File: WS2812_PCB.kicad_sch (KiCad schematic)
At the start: 4 parts, among them J1 OUT, J2 IN

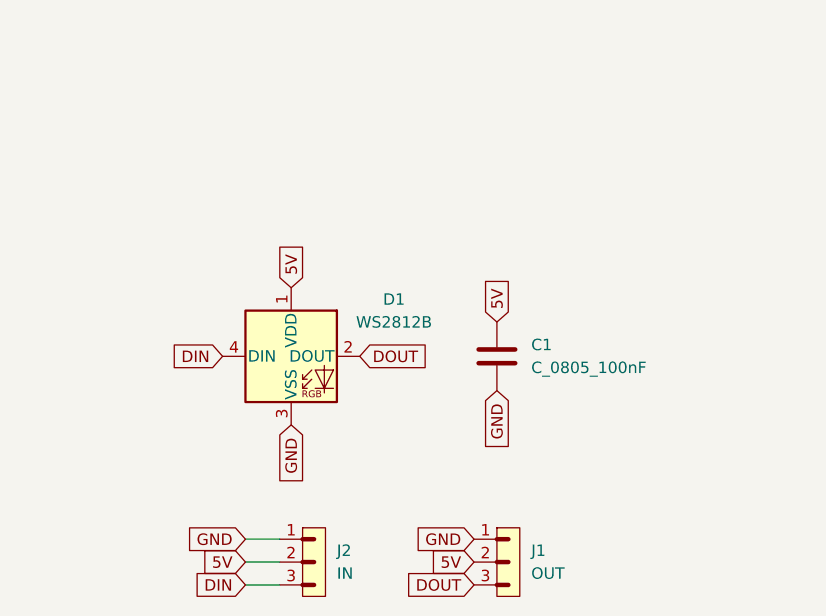
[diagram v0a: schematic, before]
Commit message: Se modifican los archivos de la pcb y esquematico para generar los archivos pdf
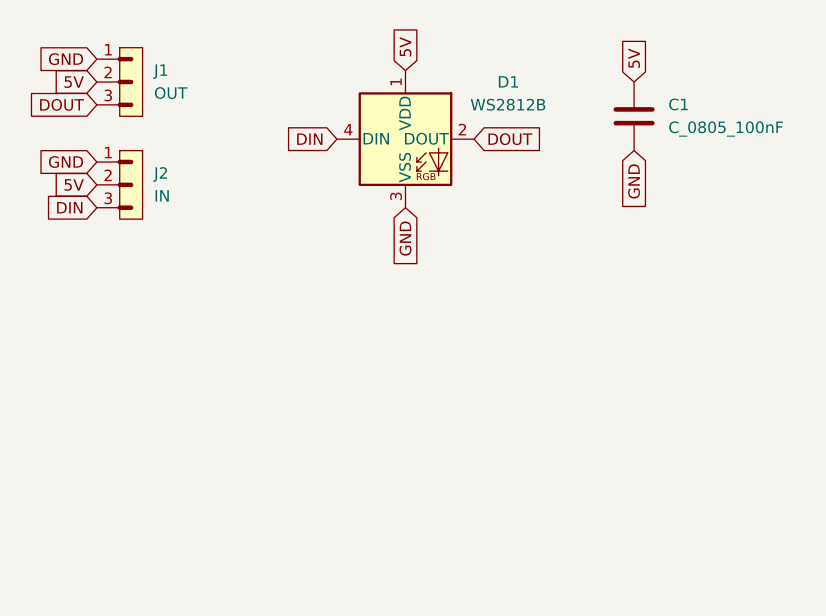
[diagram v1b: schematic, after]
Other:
- company: (none) -> Dan Angles
- title: (none) -> WS2812 PCB
- moved on the sheet: C1, D1, J1, J2
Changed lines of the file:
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@@
 	(generator "eeschema")
 	(generator_version "8.0")
-	(paper "A4")
-	(wire
-		(pts
-			(xy 58.42 80.01) (xy 62.23 80.01)
-		)
-		(stroke
-			(width 0)
-			(type default)
-		)
-	)
-	(wire
-		(pts
-			(xy 58.42 77.47) (xy 62.23 77.47)
-		)
-		(stroke
-			(width 0)
-			(type default)
-		)
-	)
-	(wire
-		(pts
-			(xy 58.42 82.55) (xy 62.23 82.55)
-		)
-		(stroke
-			(width 0)
-			(type default)
-		)
+	(paper "User" 150 100)
+	(title_block
+		(title "WS2812 PCB")
+		(date "2024-05-28")
+		(rev "1.0")
+		(company "Dan Angles")
 	)
 	(global_label "5V"
 		(shape input)
-		(at 63.5 49.53 90)
+		(at 76.2 25.4 90)
 		(fields_autoplaced yes)
 		(effects
@@
 		)
 		(property "Intersheetrefs" "${INTERSHEET_REFS}"
-			(at 63.5 44.2467 90)
+			(at 76.2 20.1167 90)
 			(effects
 				(font
@@
 	(global_label "5V"
 		(shape input)
-		(at 83.82 80.01 180)
-		(fields_autoplaced yes)
-		(effects
-			(font
-				(size 1.27 1.27)
-			)
-			(justify right)
-		)
-		(property "Intersheetrefs" "${INTERSHEET_REFS}"
-			(at 78.5367 80.01 0)
+		(at 41.91 26.67 180)
+		(fields_autoplaced yes)
+		(effects
+			(font
+				(size 1.27 1.27)
+			)
+			(justify right)
+		)
+		(property "Intersheetrefs" "${INTERSHEET_REFS}"
+			(at 36.6267 26.67 0)
 			(effects
 				(font
@@
 	(global_label "DOUT"
 		(shape input)
-		(at 71.12 57.15 0)
+		(at 83.82 33.02 0)
 		(fields_autoplaced yes)
 		(effects
@@
 		)
 		(property "Intersheetrefs" "${INTERSHEET_REFS}"
-			(at 79.0038 57.15 0)
+			(at 91.7038 33.02 0)
 			(effects
 				(font
@@
 	(global_label "5V"
 		(shape input)
-		(at 58.42 80.01 180)
-		(fields_autoplaced yes)
-		(effects
-			(font
-				(size 1.27 1.27)
-			)
-			(justify right)
-		)
-		(property "Intersheetrefs" "${INTERSHEET_REFS}"
-			(at 53.1367 80.01 0)
+		(at 41.91 38.1 180)
+		(fields_autoplaced yes)
+		(effects
+			(font
+				(size 1.27 1.27)
+			)
+			(justify right)
+		)
+		(property "Intersheetrefs" "${INTERSHEET_REFS}"
+			(at 36.6267 38.1 0)
 			(effects
 				(font
@@
 	(global_label "5V"
 		(shape input)
-		(at 86.36 53.34 90)
+		(at 101.6 26.67 90)
 		(fields_autoplaced yes)
 		(effects
@@
 		)
 		(property "Intersheetrefs" "${INTERSHEET_REFS}"
-			(at 86.36 48.0567 90)
+			(at 101.6 21.3867 90)
 			(effects
 				(font
@@
 	(global_label "DOUT"
 		(shape input)
-		(at 83.82 82.55 180)
-		(fields_autoplaced yes)
-		(effects
-			(font
-				(size 1.27 1.27)
-			)
-			(justify right)
-		)
-		(property "Intersheetrefs" "${INTERSHEET_REFS}"
-			(at 75.9362 82.55 0)
+		(at 41.91 29.21 180)
+		(fields_autoplaced yes)
+		(effects
+			(font
+				(size 1.27 1.27)
+			)
+			(justify right)
+		)
+		(property "Intersheetrefs" "${INTERSHEET_REFS}"
+			(at 34.0262 29.21 0)
 			(effects
 				(font
@@
 	(global_label "GND"
 		(shape input)
-		(at 83.82 77.47 180)
-		(fields_autoplaced yes)
-		(effects
-			(font
-				(size 1.27 1.27)
-			)
-			(justify right)
-		)
-		(property "Intersheetrefs" "${INTERSHEET_REFS}"
-			(at 76.9643 77.47 0)
+		(at 41.91 24.13 180)
+		(fields_autoplaced yes)
+		(effects
+			(font
+				(size 1.27 1.27)
+			)
+			(justify right)
+		)
+		(property "Intersheetrefs" "${INTERSHEET_REFS}"
+			(at 35.0543 24.13 0)
 			(effects
 				(font
@@
 	(global_label "GND"
 		(shape input)
-		(at 63.5 64.77 270)
-		(fields_autoplaced yes)
-		(effects
-			(font
-				(size 1.27 1.27)
-			)
-			(justify right)
-		)
-		(property "Intersheetrefs" "${INTERSHEET_REFS}"
-			(at 63.5 71.6257 90)
+		(at 76.2 40.64 270)
+		(fields_autoplaced yes)
+		(effects
+			(font
+				(size 1.27 1.27)
+			)
+			(justify right)
+		)
+		(property "Intersheetrefs" "${INTERSHEET_REFS}"
+			(at 76.2 47.4957 90)
 			(effects
 				(font
@@
 	(global_label "DIN"
 		(shape input)
-		(at 55.88 57.15 180)
-		(fields_autoplaced yes)
-		(effects
-			(font
-				(size 1.27 1.27)
-			)
-			(justify right)
-		)
-		(property "Intersheetrefs" "${INTERSHEET_REFS}"
-			(at 49.6895 57.15 0)
+		(at 68.58 33.02 180)
+		(fields_autoplaced yes)
+		(effects
+			(font
+				(size 1.27 1.27)
+			)
+			(justify right)
+		)
+		(property "Intersheetrefs" "${INTERSHEET_REFS}"
+			(at 62.3895 33.02 0)
 			(effects
 				(font
@@
 	(global_label "GND"
 		(shape input)
-		(at 58.42 77.47 180)
-		(fields_autoplaced yes)
-		(effects
-			(font
-				(size 1.27 1.27)
-			)
-			(justify right)
-		)
-		(property "Intersheetrefs" "${INTERSHEET_REFS}"
-			(at 51.5643 77.47 0)
+		(at 41.91 35.56 180)
+		(fields_autoplaced yes)
+		(effects
+			(font
+				(size 1.27 1.27)
+			)
+			(justify right)
+		)
+		(property "Intersheetrefs" "${INTERSHEET_REFS}"
+			(at 35.0543 35.56 0)
 			(effects
 				(font
@@
 	(global_label "DIN"
 		(shape input)
-		(at 58.42 82.55 180)
-		(fields_autoplaced yes)
-		(effects
-			(font
-				(size 1.27 1.27)
-			)
-			(justify right)
-		)
-		(property "Intersheetrefs" "${INTERSHEET_REFS}"
-			(at 52.2295 82.55 0)
+		(at 41.91 40.64 180)
+		(fields_autoplaced yes)
+		(effects
+			(font
+				(size 1.27 1.27)
+			)
+			(justify right)
+		)
+		(property "Intersheetrefs" "${INTERSHEET_REFS}"
+			(at 35.7195 40.64 0)
 			(effects
 				(font
@@
 	(global_label "GND"
 		(shape input)
-		(at 86.36 60.96 270)
-		(fields_autoplaced yes)
-		(effects
-			(font
-				(size 1.27 1.27)
-			)
-			(justify right)
-		)
-		(property "Intersheetrefs" "${INTERSHEET_REFS}"
-			(at 86.36 67.8157 90)
+		(at 101.6 34.29 270)
+		(fields_autoplaced yes)
+		(effects
+			(font
+				(size 1.27 1.27)
+			)
+			(justify right)
+		)
+		(property "Intersheetrefs" "${INTERSHEET_REFS}"
+			(at 101.6 41.1457 90)
 			(effects
 				(font
@@
 	(symbol
 		(lib_id "PCM_Capacitor_AKL:C_0805")
-		(at 86.36 57.15 0)
+		(at 101.6 30.48 0)
 		(unit 1)
 		(exclude_from_sim no)
@@
 		(fields_autoplaced yes)
 		(property "Reference" "C1"
-			(at 90.17 55.8799 0)
+			(at 105.41 29.2099 0)
 			(effects
 				(font
@@
 		)
 		(property "Value" "C_0805_100nF"
-			(at 90.17 58.4199 0)
+			(at 105.41 31.7499 0)
 			(effects
 				(font
@@
 		)
 		(property "Footprint" "Capacitor_SMD:C_0805_2012Metric_Pad1.18x1.45mm_HandSolder"
-			(at 87.3252 60.96 0)
+			(at 102.5652 34.29 0)
 			(effects
 				(font
@@
 		)
 		(property "Datasheet" "~"
-			(at 86.36 57.15 0)
+			(at 101.6 30.48 0)
 			(effects
 				(font
@@
 		)
 		(property "Description" "SMD 0805 MLCC capacitor, Alternate KiCad Library"
-			(at 86.36 57.15 0)
+			(at 101.6 30.48 0)
 			(effects
 				(font
@@
 	(symbol
 		(lib_id "PCM_SL_Pin_Headers:PINHD_1x3_Male")
-		(at 66.04 80.01 0)
+		(at 45.72 38.1 0)
 		(unit 1)
 		(exclude_from_sim no)
@@
 		(fields_autoplaced yes)
 		(property "Reference" "J2"
-			(at 68.58 78.7399 0)
+			(at 48.26 36.8299 0)
 			(effects
 				(font
@@
 		)
 		(property "Value" "IN"
-			(at 68.58 81.2799 0)
+			(at 48.26 39.3699 0)
 			(effects
 				(font
@@
 		)
 		(property "Footprint" "Connector_PinHeader_2.54mm:PinHeader_1x03_P2.54mm_Vertical"
-			(at 67.31 85.09 0)
+			(at 46.99 43.18 0)
 			(effects
 				(font
@@
 		)
 		(property "Datasheet" ""
-			(at 66.04 71.12 0)
+			(at 45.72 29.21 0)
 			(effects
 				(font
@@
 		)
 		(property "Description" "Pin Header male with pin space 2.54mm. Pin Count -3"
-			(at 66.04 80.01 0)
+			(at 45.72 38.1 0)
 			(effects
 				(font
@@
 	(symbol
 		(lib_id "LED:WS2812B")
-		(at 63.5 57.15 0)
+		(at 76.2 33.02 0)
 		(unit 1)
 		(exclude_from_sim no)
@@
 		(fields_autoplaced yes)
 		(property "Reference" "D1"
-			(at 74.93 50.8314 0)
+			(at 87.63 26.7014 0)
 			(effects
 				(font
@@
 		)
 		(property "Value" "WS2812B"
-			(at 74.93 53.3714 0)
+			(at 87.63 29.2414 0)
 			(effects
 				(font
@@
 		)
 		(property "Footprint" "LED_SMD:LED_WS2812B_PLCC4_5.0x5.0mm_P3.2mm"
-			(at 64.77 64.77 0)
+			(at 77.47 40.64 0)
 			(effects
 				(font
@@
 		)
 		(property "Datasheet" "https://cdn-shop.adafruit.com/datasheets/WS2812B.pdf"
-			(at 66.04 66.675 0)
+			(at 78.74 42.545 0)
 			(effects
 				(font
@@
 		)
 		(property "Description" "RGB LED with integrated controller"
-			(at 63.5 57.15 0)
+			(at 76.2 33.02 0)
 			(effects
 				(font
@@
 	(symbol
 		(lib_id "PCM_SL_Pin_Headers:PINHD_1x3_Male")
-		(at 87.63 80.01 0)
+		(at 45.72 26.67 0)
 		(unit 1)
 		(exclude_from_sim no)
@@
 		(fields_autoplaced yes)
 		(property "Reference" "J1"
-			(at 90.17 78.7399 0)
+			(at 48.26 25.3999 0)
 			(effects
 				(font
@@
 		)
 		(property "Value" "OUT"
-			(at 90.17 81.2799 0)
+			(at 48.26 27.9399 0)
 			(effects
 				(font
@@
 		)
 		(property "Footprint" "Connector_PinHeader_2.54mm:PinHeader_1x03_P2.54mm_Vertical"
-			(at 88.9 85.09 0)
+			(at 46.99 31.75 0)
 			(effects
 				(font
@@
 		)
 		(property "Datasheet" ""
-			(at 87.63 71.12 0)
+			(at 45.72 17.78 0)
 			(effects
 				(font
@@
 		)
 		(property "Description" "Pin Header male with pin space 2.54mm. Pin Count -3"
-			(at 87.63 80.01 0)
-			(effects
-				(font
+			(at 45.72 26.67 0)
+			(effects
+				(font
